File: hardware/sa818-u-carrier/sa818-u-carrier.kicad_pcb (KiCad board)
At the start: 2 copper layers, 120 x 40 mm, 9 parts, among them J18 Conn_Coaxial, J19 Power/Audio, J20 Control/Data, J21 Conn_01x03_Pin, J22 Conn_01x03_Pin, U10 SA818U

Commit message: UHF carrier board
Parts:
- renumbered J19 to J18, J18 to J19
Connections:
- J20 pad 7: Net-(J20-Pin_7) -> unconnected-(J20-Pin_7-Pad7)
- J21 pad 1: GND -> unconnected-(J21-Pin_1-Pad1)
- J21 pad 2: GND -> unconnected-(J21-Pin_2-Pad2)
- J22 pad 3: GND -> unconnected-(J22-Pin_3-Pad3)
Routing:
- net Net-(J20-Pin_7): track 10.2 -> 0.00 mm
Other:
- board text added: "HAM RADIO VILLAGE SSTV BADGE (UHF) SEND ME YOUR MEMES OR POSE FOR A SELFIE JOIN US! https://hamvillage.org"
- board text removed: "HAM RADIO VILLAGE SSTV BADGE (VHF) SEND ME YOUR MEMES OR POSE FOR A SELFIE JOIN US! https://hamvillage.org"

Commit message: update text on carrier boards
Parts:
- J18, J20, J21, J22: moved to B.Cu
- moved J21 106.0 mm to (193.0, 53.0)
- moved J22 106.0 mm to (87.0, 53.0)
- moved J18 56.0 mm to (168.0, 87.0)
- moved J20 56.0 mm to (112.0, 87.0)
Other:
- board text added: "HAM RADIO VILLAGE SSTV BADGE (UHF) JOIN US! https://www.hamvillage.org"
- board text added: "HRV SSTV BADGE"
- board text added: "SEND ME UR MEMES!"
- board text added: "UHF CARRIER BOARD Rev 0.1"
- board text removed: "HAM RADIO VILLAGE SSTV BADGE (UHF) SEND ME YOUR MEMES OR POSE FOR A SELFIE JOIN US! https://hamvillage.org"
- board text removed: "HRV SSTV BADGE UHF CARRIER BOARD REV 0.1"

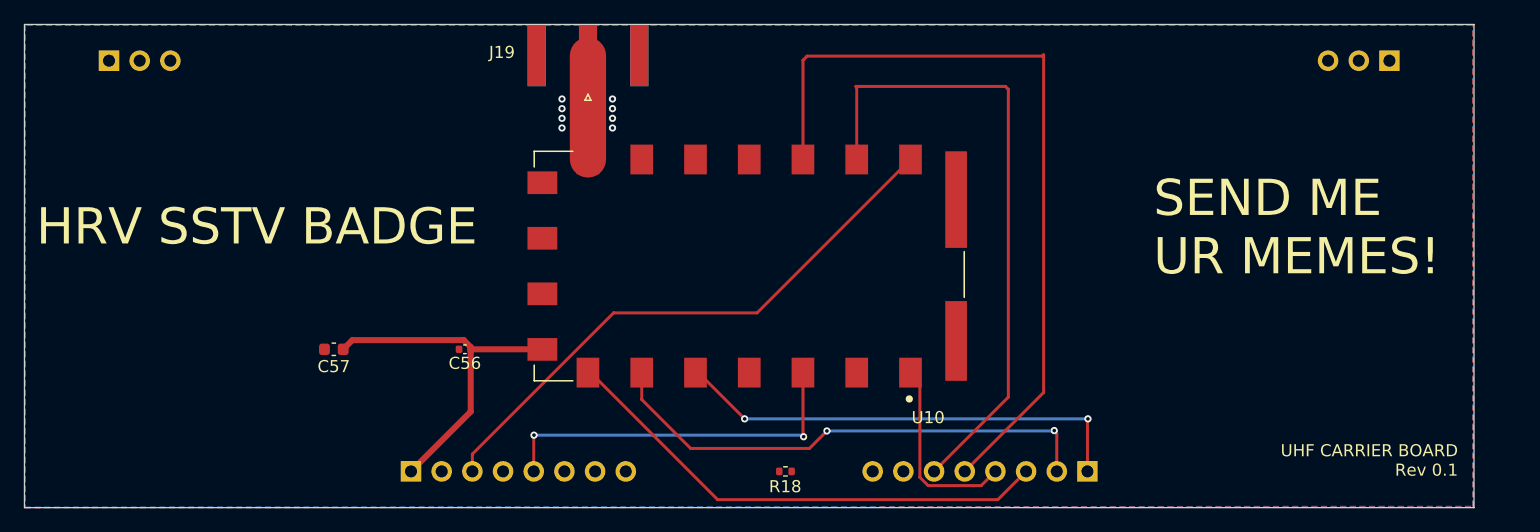
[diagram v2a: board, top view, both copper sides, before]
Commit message: routing and component bug fixes
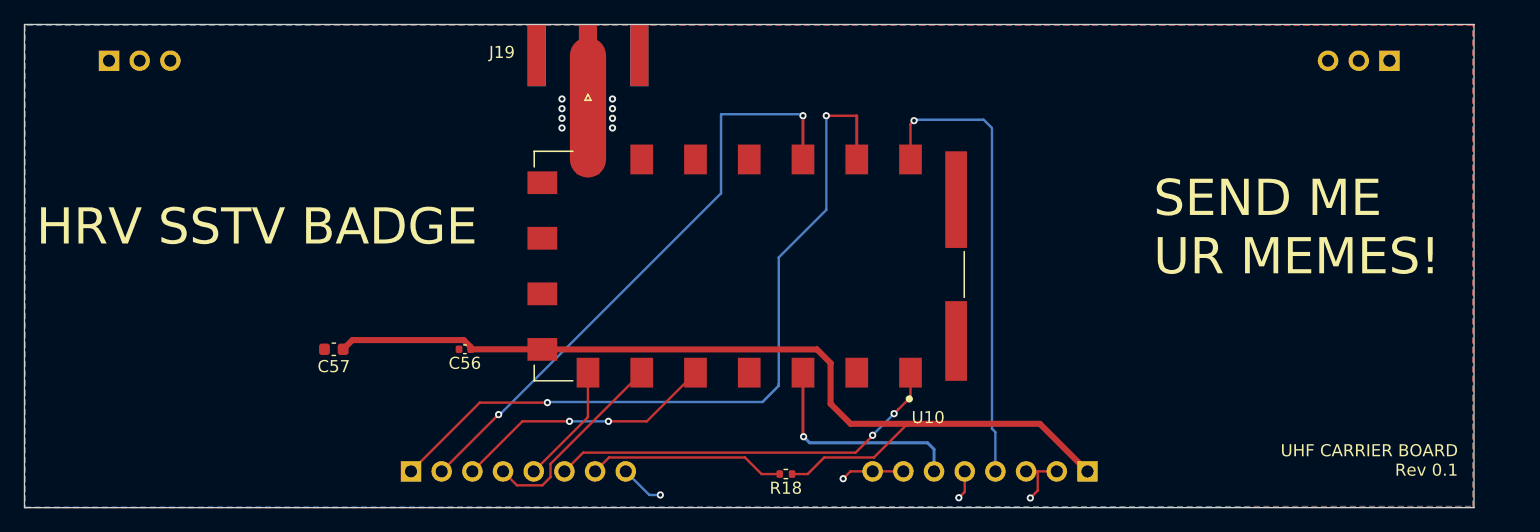
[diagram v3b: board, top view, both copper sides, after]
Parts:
- R18: value 0 -> 10k
- moved R18 0.22 mm to (143.0, 87.2)
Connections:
- J18 pad 3: Net-(J18-Pin_3) -> GND
- J18 pad 4: GND -> Net-(J18-Pin_4)
- J18 pad 5: Net-(J18-Pin_5) -> GND
- J18 pad 6: GND -> Net-(J18-Pin_6)
- J20 pad 7: unconnected-(J20-Pin_7-Pad7) -> Net-(J20-Pin_7)
- J21 pad 1: unconnected-(J21-Pin_1-Pad1) -> GND
- J21 pad 2: unconnected-(J21-Pin_2-Pad2) -> GND
- J22 pad 3: unconnected-(J22-Pin_3-Pad3) -> GND
- R18 pad 1: Net-(J20-Pin_7) -> Net-(J18-Pin_1)
- R18 pad 2: GND -> Net-(J20-Pin_7)
- U10 pad 1: Net-(J20-Pin_4) -> Net-(J20-Pin_6)
- U10 pad 16: Net-(J20-Pin_5) -> Net-(J20-Pin_2)
- U10 pad 17: Net-(J20-Pin_6) -> Net-(J20-Pin_1)
- U10 pad 18: Net-(J18-Pin_3) -> Net-(J18-Pin_4)
- U10 pad 3: Net-(J18-Pin_5) -> Net-(J18-Pin_6)
- U10 pad 5: Net-(J20-Pin_1) -> Net-(J20-Pin_3)
- U10 pad 6: Net-(J20-Pin_2) -> Net-(J20-Pin_4)
- U10 pad 7: Net-(J20-Pin_3) -> Net-(J20-Pin_5)
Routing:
- net Net-(J20-Pin_5): track 65.5 -> 10.3 mm
- net Net-(J18-Pin_1): track 29.4 -> 79.8 mm
- net Net-(J18-Pin_3): track 47.8 -> 0.00 mm
- net Net-(J18-Pin_4): track 0.00 -> 39.0 mm, vias 0 -> 1
- net Net-(J18-Pin_5): track 30.7 -> 0.00 mm, vias 2 -> 0
- net Net-(J20-Pin_1): track 38.4 -> 63.5 mm
- net Net-(J20-Pin_3): track 41.6 -> 22.1 mm, vias 0 -> 2
- net Net-(J20-Pin_6): track 53.0 -> 34.3 mm, vias 0 -> 2
- net Net-(J18-Pin_6): track 0.00 -> 18.4 mm, vias 0 -> 1
- net Net-(J20-Pin_7): track 0.00 -> 17.1 mm
- net GND: track 0.00 -> 16.3 mm, vias 8 -> 12
- net Net-(J20-Pin_2): track 42.1 -> 49.7 mm
